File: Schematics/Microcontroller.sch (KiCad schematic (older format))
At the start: 21 parts, among them CON301 USB-MICRO-B, IC301 ATXMEGA256A3BU-A, J301 AVR_JTAG_Header, X301 12MHz, X302 32.768KhZ

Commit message: LEDs are placed!
Worked out how to script KiCAD to do it too. Winner winner, time for a chicken dinner
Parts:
- renumbered BT301 to BT1, C301 to C10, C302 to C11, C303 to C12, C304 to C13, C305 to C14, C306 to C15, C307 to C16, C308 to C17, C309 to C18, C310 to C19, C311 to C20, CON301 to CON1, IC301 to IC1, J301 to J1, R301 to R15, R302 to R16, R303 to R17, R304 to R18, X301 to X1, X302 to X2
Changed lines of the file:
@@
 $EndDescr
 $Comp
-L ATXMEGA256A3BU-A IC301
+L ATXMEGA256A3BU-A IC1
 U 1 1 54B11B55
 P 5850 3550
-F 0 "IC301" H 4900 5350 40  0000 L BNN
+F 0 "IC1" H 4900 5350 40  0000 L BNN
 F 1 "ATXMEGA256A3BU-A" H 6250 1650 40  0000 L BNN
 F 2 "SMD_Packages:TQFP-64" H 5850 3550 35  0000 C CIN
@@
 $EndComp
 $Comp
-L AVR_JTAG_Header J301
+L AVR_JTAG_Header J1
 U 1 1 54B11B88
 P 9350 3150
-F 0 "J301" H 9150 3550 60  0000 C CNN
+F 0 "J1" H 9150 3550 60  0000 C CNN
 F 1 "AVR_JTAG_Header" H 9900 2850 60  0000 C CNN
 F 2 "Socket_Strips:Socket_Strip_Straight_2x05" H 9350 3150 60  0001 C CNN
@@
 $EndComp
 $Comp
-L R R303
+L R R17
 U 1 1 54B11BE7
 P 9050 1550
-F 0 "R303" V 9130 1550 40  0000 C CNN
+F 0 "R17" V 9130 1550 40  0000 C CNN
 F 1 "47k" V 9057 1551 40  0000 C CNN
 F 2 "Resistors_SMD:R_0603" V 8980 1550 30  0001 C CNN
@@
 $EndComp
 $Comp
-L R R304
+L R R18
 U 1 1 54B11C1B
 P 9400 1550
-F 0 "R304" V 9480 1550 40  0000 C CNN
+F 0 "R18" V 9480 1550 40  0000 C CNN
 F 1 "47k" V 9407 1551 40  0000 C CNN
 F 2 "Resistors_SMD:R_0603" V 9330 1550 30  0001 C CNN
@@
 	4250 1950 4750 1950
 $Comp
-L CRYSTAL X302
+L CRYSTAL X2
 U 1 1 54B1373C
 P 3800 2550
-F 0 "X302" H 3800 2700 60  0000 C CNN
+F 0 "X2" H 3800 2700 60  0000 C CNN
 F 1 "32.768KhZ" H 3800 2400 60  0000 C CNN
 F 2 "" H 3800 2550 60  0001 C CNN
@@
 $EndComp
 $Comp
-L C C304
+L C C13
 U 1 1 54B13791
 P 4200 2800
-F 0 "C304" H 4200 2900 40  0000 L CNN
+F 0 "C13" H 4200 2900 40  0000 L CNN
 F 1 "C" H 4206 2715 40  0000 L CNN
 F 2 "Capacitors_SMD:C_0603" H 4238 2650 30  0001 C CNN
@@
 $EndComp
 $Comp
-L C C302
+L C C11
 U 1 1 54B137B6
 P 3400 2800
-F 0 "C302" H 3400 2900 40  0000 L CNN
+F 0 "C11" H 3400 2900 40  0000 L CNN
 F 1 "C" H 3406 2715 40  0000 L CNN
 F 2 "Capacitors_SMD:C_0603" H 3438 2650 30  0001 C CNN
@@
 	3400 3100 3400 3000
 $Comp
-L CRYSTAL X301
+L CRYSTAL X1
 U 1 1 54B13F67
 P 3550 3650
-F 0 "X301" H 3550 3800 60  0000 C CNN
+F 0 "X1" H 3550 3800 60  0000 C CNN
 F 1 "12MHz" H 3550 3500 60  0000 C CNN
 F 2 "" H 3550 3650 60  0001 C CNN
@@
 $EndComp
 $Comp
-L C C303
+L C C12
 U 1 1 54B13F6D
 P 3950 3900
-F 0 "C303" H 3950 4000 40  0000 L CNN
+F 0 "C12" H 3950 4000 40  0000 L CNN
 F 1 "C" H 3956 3815 40  0000 L CNN
 F 2 "Capacitors_SMD:C_0603" H 3988 3750 30  0001 C CNN
@@
 $EndComp
 $Comp
-L C C301
+L C C10
 U 1 1 54B13F73
 P 3150 3900
-F 0 "C301" H 3150 4000 40  0000 L CNN
+F 0 "C10" H 3150 4000 40  0000 L CNN
 F 1 "C" H 3156 3815 40  0000 L CNN
 F 2 "Capacitors_SMD:C_0603" H 3188 3750 30  0001 C CNN
@@
 USB_D-
 $Comp
-L USB-MICRO-B CON301
+L USB-MICRO-B CON1
 U 1 1 54B1509B
 P 9900 5550
-F 0 "CON301" H 9600 5900 50  0000 C CNN
+F 0 "CON1" H 9600 5900 50  0000 C CNN
 F 1 "USB-MICRO-B" H 9750 5200 50  0000 C CNN
 F 2 "Connect:USB_Micro-B" H 9900 5450 50  0001 C CNN
@@
 USB_D-
 $Comp
-L BATTERY BT301
+L BATTERY BT1
 U 1 1 54B172FA
 P 3600 2100
-F 0 "BT301" H 3600 2300 50  0000 C CNN
+F 0 "BT1" H 3600 2300 50  0000 C CNN
 F 1 "3V" H 3600 1910 50  0000 C CNN
 F 2 "" H 3600 2100 60  0001 C CNN
@@
 $EndComp
 $Comp
-L R R301
+L R R15
 U 1 1 54B17628
 P 4350 2250
-F 0 "R301" V 4430 2250 40  0000 C CNN
+F 0 "R15" V 4430 2250 40  0000 C CNN
 F 1 "100R" V 4357 2251 40  0000 C CNN
 F 2 "Resistors_SMD:R_0603" V 4280 2250 30  0001 C CNN
@@
 NoConn ~ 4750 2050
 $Comp
-L R R302
+L R R16
 U 1 1 54B182E1
 P 7200 1000
-F 0 "R302" V 7280 1000 40  0000 C CNN
+F 0 "R16" V 7280 1000 40  0000 C CNN
 F 1 "50R" V 7207 1001 40  0000 C CNN
 F 2 "Resistors_SMD:R_0603" V 7130 1000 30  0001 C CNN
@@
 ~OE[1..12]
 $Comp
-L C C306
+L C C15
 U 1 1 54B28316
 P 4500 1200
-F 0 "C306" H 4500 1300 40  0000 L CNN
+F 0 "C15" H 4500 1300 40  0000 L CNN
 F 1 "100n" H 4506 1115 40  0000 L CNN
 F 2 "Capacitors_SMD:C_0603" H 4538 1050 30  0001 C CNN
@@
 $EndComp
 $Comp
-L C C307
+L C C16
 U 1 1 54B28394
 P 4750 1200
-F 0 "C307" H 4750 1300 40  0000 L CNN
+F 0 "C16" H 4750 1300 40  0000 L CNN
 F 1 "100n" H 4756 1115 40  0000 L CNN
 F 2 "Capacitors_SMD:C_0603" H 4788 1050 30  0001 C CNN
@@
 $EndComp
 $Comp
-L C C308
+L C C17
 U 1 1 54B283DE
 P 5000 1200
-F 0 "C308" H 5000 1300 40  0000 L CNN
+F 0 "C17" H 5000 1300 40  0000 L CNN
 F 1 "100n" H 5006 1115 40  0000 L CNN
 F 2 "Capacitors_SMD:C_0603" H 5038 1050 30  0001 C CNN
@@
 $EndComp
 $Comp
-L C C309
+L C C18
 U 1 1 54B28409
 P 5250 1200
-F 0 "C309" H 5250 1300 40  0000 L CNN
+F 0 "C18" H 5250 1300 40  0000 L CNN
 F 1 "100n" H 5256 1115 40  0000 L CNN
 F 2 "Capacitors_SMD:C_0603" H 5288 1050 30  0001 C CNN
@@
 $EndComp
 $Comp
-L C C310
+L C C19
 U 1 1 54B28435
 P 5500 1200
-F 0 "C310" H 5500 1300 40  0000 L CNN
+F 0 "C19" H 5500 1300 40  0000 L CNN
 F 1 "100n" H 5506 1115 40  0000 L CNN
 F 2 "Capacitors_SMD:C_0603" H 5538 1050 30  0001 C CNN
@@
 $EndComp
 $Comp
-L C C305
+L C C14
 U 1 1 54B28462
 P 4250 1200
-F 0 "C305" H 4250 1300 40  0000 L CNN
+F 0 "C14" H 4250 1300 40  0000 L CNN
 F 1 "1u" H 4256 1115 40  0000 L CNN
 F 2 "Capacitors_SMD:C_0603" H 4288 1050 30  0001 C CNN
@@
 Connection ~ 4250 1500
 $Comp
-L C C311
+L C C20
 U 1 1 54B28ED0
 P 8700 5600
-F 0 "C311" H 8700 5700 40  0000 L CNN
+F 0 "C20" H 8700 5700 40  0000 L CNN
 F 1 "1u" H 8706 5515 40  0000 L CNN
 F 2 "Capacitors_SMD:C_0603" H 8738 5450 30  0001 C CNN

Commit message: Latest schematics and pcb.
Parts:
- removed X1: 12MHz, symbol CRYSTAL
- removed X2: 32.768KhZ, symbol CRYSTAL
- added JP1: JUMPER, symbol JUMPER
- added R100: 100k, Resistors_SMD:R_0603, symbol R
- added X1: 12MHz, symbol CRYSTAL_SMD
- added X2: 32.768KhZ, symbol CRYSTAL_SMD
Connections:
- wire segments 108 -> 115
- no-connect marks 25 -> 23
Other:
- moved on the sheet: R16
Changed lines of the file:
@@
 	4250 1950 4750 1950
-$Comp
-L CRYSTAL X2
-U 1 1 54B1373C
-P 3800 2550
-F 0 "X2" H 3800 2700 60  0000 C CNN
-F 1 "32.768KhZ" H 3800 2400 60  0000 C CNN
-F 2 "" H 3800 2550 60  0001 C CNN
-F 3 "" H 3800 2550 60  0000 C CNN
-	1    3800 2550
-	1    0    0    -1
-$EndComp
 $Comp
 L C C13
@@
 $EndComp
 Wire Wire Line
-	4100 2550 4750 2550
+	4000 2550 4750 2550
 Connection ~ 4200 2550
 Wire Wire Line
@@
 	3400 2600 3400 2550
 Wire Wire Line
-	3250 2550 3500 2550
+	3250 2550 3600 2550
 Connection ~ 3400 2550
 Text Label 4500 2750 0    60   ~ 0
@@
 	3400 3100 3400 3000
 $Comp
-L CRYSTAL X1
-U 1 1 54B13F67
-P 3550 3650
-F 0 "X1" H 3550 3800 60  0000 C CNN
-F 1 "12MHz" H 3550 3500 60  0000 C CNN
-F 2 "" H 3550 3650 60  0001 C CNN
-F 3 "" H 3550 3650 60  0000 C CNN
-	1    3550 3650
-	1    0    0    -1
-$EndComp
-$Comp
 L C C12
 U 1 1 54B13F6D
@@
 	3150 3700 3150 3650
 Wire Wire Line
-	3000 3650 3250 3650
+	3000 3650 3350 3650
 Connection ~ 3150 3650
 $Comp
@@
 	3150 4200 3150 4100
 Wire Wire Line
-	3850 3650 4450 3650
+	3750 3650 4450 3650
 Wire Wire Line
 	4450 3650 4450 3400
@@
 L R R16
 U 1 1 54B182E1
-P 7200 1000
-F 0 "R16" V 7280 1000 40  0000 C CNN
-F 1 "50R" V 7207 1001 40  0000 C CNN
-F 2 "Resistors_SMD:R_0603" V 7130 1000 30  0001 C CNN
-F 3 "" H 7200 1000 30  0000 C CNN
-	1    7200 1000
-	1    0    0    -1
-$EndComp
-Text HLabel 7500 700  2    60   Input ~ 0
+P 7850 1000
+F 0 "R16" V 7930 1000 40  0000 C CNN
+F 1 "50R" V 7857 1001 40  0000 C CNN
+F 2 "Resistors_SMD:R_0603" V 7780 1000 30  0001 C CNN
+F 3 "" H 7850 1000 30  0000 C CNN
+	1    7850 1000
+	1    0    0    -1
+$EndComp
+Text HLabel 8150 700  2    60   Input ~ 0
 RF_In
 $Comp
 L GND #PWR030
 U 1 1 54B18749
-P 7200 1300
-F 0 "#PWR030" H 7200 1050 60  0001 C CNN
-F 1 "GND" H 7200 1150 60  0000 C CNN
-F 2 "" H 7200 1300 60  0000 C CNN
-F 3 "" H 7200 1300 60  0000 C CNN
-	1    7200 1300
-	1    0    0    -1
-$EndComp
-Wire Wire Line
-	6950 1950 7450 1950
-Wire Wire Line
-	7050 700  7500 700
-Wire Wire Line
-	7200 750  7200 700
-Connection ~ 7200 700
-Text Label 7050 700  2    60   ~ 0
+P 7850 1300
+F 0 "#PWR030" H 7850 1050 60  0001 C CNN
+F 1 "GND" H 7850 1150 60  0000 C CNN
+F 2 "" H 7850 1300 60  0000 C CNN
+F 3 "" H 7850 1300 60  0000 C CNN
+	1    7850 1300
+	1    0    0    -1
+$EndComp
+Wire Wire Line
+	7700 700  8150 700
+Wire Wire Line
+	7850 750  7850 700
+Connection ~ 7850 700
+Text Label 7700 700  2    60   ~ 0
 RF_In
-Text Label 7450 1950 2    60   ~ 0
+Text Label 7400 2650 2    60   ~ 0
 RF_In
 Wire Wire Line
-	7200 1300 7200 1250
+	7850 1300 7850 1250
 NoConn ~ 6950 2050
 NoConn ~ 6950 2150
-NoConn ~ 6950 2250
 NoConn ~ 6950 2350
 NoConn ~ 6950 2450
 NoConn ~ 6950 2550
-NoConn ~ 6950 2650
 NoConn ~ 6950 2800
 NoConn ~ 6950 2900
@@
 NoConn ~ 4750 4800
 NoConn ~ 4750 4900
-NoConn ~ 4750 5000
 Text Label 8050 5100 2    60   ~ 0
 ~OE[1..12]
@@
 	8700 5800 9250 5800
 Connection ~ 9250 5800
+$Comp
+L CRYSTAL_SMD X2
+U 1 1 54B2624B
+P 3800 2550
+F 0 "X2" H 3800 2640 30  0000 C CNN
+F 1 "32.768KhZ" H 3830 2440 30  0000 L CNN
+F 2 "" H 3800 2550 60  0000 C CNN
+F 3 "" H 3800 2550 60  0000 C CNN
+	1    3800 2550
+	1    0    0    -1
+$EndComp
+$Comp
+L GND #PWR033
+U 1 1 54B26812
+P 3800 2700
+F 0 "#PWR033" H 3800 2450 60  0001 C CNN
+F 1 "GND" H 3800 2550 60  0000 C CNN
+F 2 "" H 3800 2700 60  0000 C CNN
+F 3 "" H 3800 2700 60  0000 C CNN
+	1    3800 2700
+	1    0    0    -1
+$EndComp
+Wire Wire Line
+	3800 2700 3800 2650
+$Comp
+L CRYSTAL_SMD X1
+U 1 1 54B26940
+P 3550 3650
+F 0 "X1" H 3550 3740 30  0000 C CNN
+F 1 "12MHz" H 3580 3540 30  0000 L CNN
+F 2 "" H 3550 3650 60  0000 C CNN
+F 3 "" H 3550 3650 60  0000 C CNN
+	1    3550 3650
+	1    0    0    -1
+$EndComp
+$Comp
+L GND #PWR034
+U 1 1 54B26B40
+P 3550 3850
+F 0 "#PWR034" H 3550 3600 60  0001 C CNN
+F 1 "GND" H 3550 3700 60  0000 C CNN
+F 2 "" H 3550 3850 60  0000 C CNN
+F 3 "" H 3550 3850 60  0000 C CNN
+	1    3550 3850
+	1    0    0    -1
+$EndComp
+Wire Wire Line
+	3550 3850 3550 3750
+Wire Wire Line
+	6950 2650 7400 2650
+$Comp
+L JUMPER JP1
+U 1 1 54B2854F
+P 7450 2250
+F 0 "JP1" H 7450 2400 60  0000 C CNN
+F 1 "JUMPER" H 7450 2170 40  0000 C CNN
+F 2 "" H 7450 2250 60  0000 C CNN
+F 3 "" H 7450 2250 60  0000 C CNN
+	1    7450 2250
+	1    0    0    -1
+$EndComp
+NoConn ~ 6950 1950
+$Comp
+L GND #PWR035
+U 1 1 54B2A340
+P 7800 2350
+F 0 "#PWR035" H 7800 2100 60  0001 C CNN
+F 1 "GND" H 7800 2200 60  0000 C CNN
+F 2 "" H 7800 2350 60  0000 C CNN
+F 3 "" H 7800 2350 60  0000 C CNN
+	1    7800 2350
+	1    0    0    -1
+$EndComp
+$Comp
+L R R100
+U 1 1 54B2AC08
+P 7100 1950
+F 0 "R100" V 7180 1950 40  0000 C CNN
+F 1 "100k" V 7107 1951 40  0000 C CNN
+F 2 "Resistors_SMD:R_0603" V 7030 1950 30  0001 C CNN
+F 3 "" H 7100 1950 30  0000 C CNN
+	1    7100 1950
+	1    0    0    -1
+$EndComp
+$Comp
+L VPP #PWR036
+U 1 1 54B2B24F
+P 7100 1650
+F 0 "#PWR036" H 7100 1500 60  0001 C CNN
+F 1 "VPP" H 7100 1800 60  0000 C CNN
+F 2 "" H 7100 1650 60  0000 C CNN
+F 3 "" H 7100 1650 60  0000 C CNN
+	1    7100 1650
+	1    0    0    -1
+$EndComp
+Wire Wire Line
+	7100 1700 7100 1650
+Wire Wire Line
+	6950 2250 7150 2250
+Wire Wire Line
+	7100 2200 7100 2250
+Connection ~ 7100 2250
+Wire Wire Line
+	7800 2350 7800 2250
+Wire Wire Line
+	7800 2250 7750 2250
 $EndSCHEMATC

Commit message: Updated schematics
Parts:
- removed R16: 50R, Resistors_SMD:R_0603, symbol R
- added P?: CONN_02X08, symbol CONN_02X08
- BT1: footprint (none) -> rgb:BU2032SM-HD-GTR-ND
- CON1: footprint Connect:USB_Micro-B -> usb:USB_Micro-B
- IC1: footprint SMD_Packages:TQFP-64 -> Housings_QFP:TQFP-64_14x14mm_Pitch0.8mm
- J1: footprint Socket_Strips:Socket_Strip_Straight_2x05 -> rgb:FTSH-105-01-L-DV-K-A-P
- JP1: footprint (none) -> SMD_Packages:SMD-0201_r
- X1, X2: footprint (none) -> Crystals_Oscillators_SMD:crystal_FA238-TSX3225
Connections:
- net labels added: MISO, MOSI, RX, SCK, TX, Vusb, ~CS
- net labels removed: RF_In
- wire segments 115 -> 126
- no-connect marks 23 -> 20
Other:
- moved on the sheet: C10, C12, JP1, R100, X1

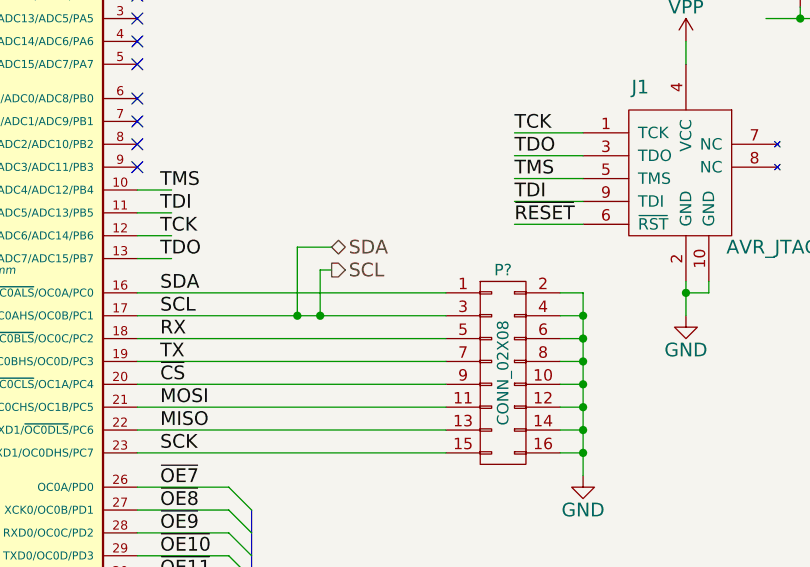
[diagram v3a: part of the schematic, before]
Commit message: Removed RF. Placed all LED drivers and passives and begun routing
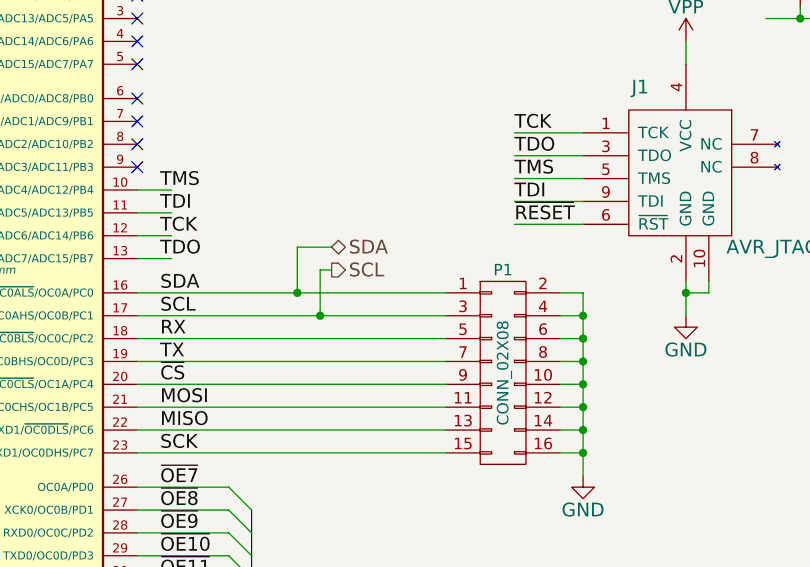
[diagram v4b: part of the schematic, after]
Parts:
- gave numbers to parts that had none: 1
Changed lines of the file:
@@
 SCL
 $Comp
-L VPP #PWR019
+L VPP #PWR02
 U 1 1 54B121F9
 P 9250 1200
-F 0 "#PWR019" H 9250 1050 60  0001 C CNN
+F 0 "#PWR02" H 9250 1050 60  0001 C CNN
 F 1 "VPP" H 9250 1350 60  0000 C CNN
 F 2 "" H 9250 1200 60  0000 C CNN
@@
 $EndComp
 $Comp
-L VPP #PWR020
+L VPP #PWR03
 U 1 1 54B1220F
 P 5800 1450
-F 0 "#PWR020" H 5800 1300 60  0001 C CNN
+F 0 "#PWR03" H 5800 1300 60  0001 C CNN
 F 1 "VPP" H 5800 1600 60  0000 C CNN
 F 2 "" H 5800 1450 60  0000 C CNN
@@
 $EndComp
 $Comp
-L GND #PWR021
+L GND #PWR04
 U 1 1 54B12386
 P 5850 5600
-F 0 "#PWR021" H 5850 5350 60  0001 C CNN
+F 0 "#PWR04" H 5850 5350 60  0001 C CNN
 F 1 "GND" H 5850 5450 60  0000 C CNN
 F 2 "" H 5850 5600 60  0000 C CNN
@@
 TMS
 $Comp
-L VPP #PWR022
+L VPP #PWR05
 U 1 1 54B12F47
 P 9350 2550
-F 0 "#PWR022" H 9350 2400 60  0001 C CNN
+F 0 "#PWR05" H 9350 2400 60  0001 C CNN
 F 1 "VPP" H 9350 2700 60  0000 C CNN
 F 2 "" H 9350 2550 60  0000 C CNN
@@
 $EndComp
 $Comp
-L GND #PWR023
+L GND #PWR06
 U 1 1 54B12FD2
 P 9350 3750
-F 0 "#PWR023" H 9350 3500 60  0001 C CNN
+F 0 "#PWR06" H 9350 3500 60  0001 C CNN
 F 1 "GND" H 9350 3600 60  0000 C CNN
 F 2 "" H 9350 3750 60  0000 C CNN
@@
 TOSC1
 $Comp
-L GND #PWR024
+L GND #PWR07
 U 1 1 54B13B7D
 P 3400 3100
-F 0 "#PWR024" H 3400 2850 60  0001 C CNN
+F 0 "#PWR07" H 3400 2850 60  0001 C CNN
 F 1 "GND" H 3400 2950 60  0000 C CNN
 F 2 "" H 3400 3100 60  0000 C CNN
@@
 $EndComp
 $Comp
-L GND #PWR025
+L GND #PWR08
 U 1 1 54B13BA4
 P 4200 3100
-F 0 "#PWR025" H 4200 2850 60  0001 C CNN
+F 0 "#PWR08" H 4200 2850 60  0001 C CNN
 F 1 "GND" H 4200 2950 60  0000 C CNN
 F 2 "" H 4200 3100 60  0000 C CNN
@@
 $EndComp
 $Comp
-L GND #PWR026
+L GND #PWR09
 U 1 1 54B13F80
 P 3150 3900
-F 0 "#PWR026" H 3150 3650 60  0001 C CNN
+F 0 "#PWR09" H 3150 3650 60  0001 C CNN
 F 1 "GND" H 3150 3750 60  0000 C CNN
 F 2 "" H 3150 3900 60  0000 C CNN
@@
 $EndComp
 $Comp
-L GND #PWR027
+L GND #PWR010
 U 1 1 54B13F86
 P 3950 3900
-F 0 "#PWR027" H 3950 3650 60  0001 C CNN
+F 0 "#PWR010" H 3950 3650 60  0001 C CNN
 F 1 "GND" H 3950 3750 60  0000 C CNN
 F 2 "" H 3950 3900 60  0000 C CNN
@@
 $EndComp
 $Comp
-L GND #PWR028
+L GND #PWR011
 U 1 1 54B15BE6
 P 9250 5850
-F 0 "#PWR028" H 9250 5600 60  0001 C CNN
+F 0 "#PWR011" H 9250 5600 60  0001 C CNN
 F 1 "GND" H 9250 5700 60  0000 C CNN
 F 2 "" H 9250 5850 60  0000 C CNN
@@
 $EndComp
 $Comp
-L GND #PWR029
+L GND #PWR012
 U 1 1 54B15BFC
 P 10450 5850
-F 0 "#PWR029" H 10450 5600 60  0001 C CNN
+F 0 "#PWR012" H 10450 5600 60  0001 C CNN
 F 1 "GND" H 10450 5700 60  0000 C CNN
 F 2 "" H 10450 5850 60  0000 C CNN
@@
 $EndComp
 $Comp
-L GND #PWR030
+L GND #PWR013
 U 1 1 54B17721
 P 3200 2200
-F 0 "#PWR030" H 3200 1950 60  0001 C CNN
+F 0 "#PWR013" H 3200 1950 60  0001 C CNN
 F 1 "GND" H 3200 2050 60  0000 C CNN
 F 2 "" H 3200 2200 60  0000 C CNN
@@
 $EndComp
 $Comp
-L VPP #PWR032
+L VPP #PWR014
 U 1 1 54B284BD
 P 4900 900
-F 0 "#PWR032" H 4900 750 60  0001 C CNN
+F 0 "#PWR014" H 4900 750 60  0001 C CNN
 F 1 "VPP" H 4900 1050 60  0000 C CNN
 F 2 "" H 4900 900 60  0000 C CNN
@@
 $EndComp
 $Comp
-L GND #PWR033
+L GND #PWR015
 U 1 1 54B28C09
 P 4250 1600
-F 0 "#PWR033" H 4250 1350 60  0001 C CNN
+F 0 "#PWR015" H 4250 1350 60  0001 C CNN
 F 1 "GND" H 4250 1450 60  0000 C CNN
 F 2 "" H 4250 1600 60  0000 C CNN
@@
 $EndComp
 $Comp
-L GND #PWR034
+L GND #PWR016
 U 1 1 54B26812
 P 3800 2700
-F 0 "#PWR034" H 3800 2450 60  0001 C CNN
+F 0 "#PWR016" H 3800 2450 60  0001 C CNN
 F 1 "GND" H 3800 2550 60  0000 C CNN
 F 2 "" H 3800 2700 60  0000 C CNN
@@
 $EndComp
 $Comp
-L GND #PWR035
+L GND #PWR017
 U 1 1 54B26B40
 P 3550 3600
-F 0 "#PWR035" H 3550 3350 60  0001 C CNN
+F 0 "#PWR017" H 3550 3350 60  0001 C CNN
 F 1 "GND" H 3550 3450 60  0000 C CNN
 F 2 "" H 3550 3600 60  0000 C CNN
@@
 $EndComp
 $Comp
-L GND #PWR036
+L GND #PWR018
 U 1 1 54B2A340
 P 10550 2550
-F 0 "#PWR036" H 10550 2300 60  0001 C CNN
+F 0 "#PWR018" H 10550 2300 60  0001 C CNN
 F 1 "GND" H 10550 2400 60  0000 C CNN
 F 2 "" H 10550 2550 60  0000 C CNN
@@
 $EndComp
 $Comp
-L VPP #PWR037
+L VPP #PWR019
 U 1 1 54B2B24F
 P 9850 1850
-F 0 "#PWR037" H 9850 1700 60  0001 C CNN
+F 0 "#PWR019" H 9850 1700 60  0001 C CNN
 F 1 "VPP" H 9850 2000 60  0000 C CNN
 F 2 "" H 9850 1850 60  0000 C CNN
@@
 NoConn ~ 6950 1950
 $Comp
-L CONN_02X08 P?
+L CONN_02X08 P1
 U 1 1 54C8095F
 P 8550 4000
-F 0 "P?" H 8550 4450 50  0000 C CNN
+F 0 "P1" H 8550 4450 50  0000 C CNN
 F 1 "CONN_02X08" V 8550 4000 50  0000 C CNN
 F 2 "" H 8550 2800 60  0000 C CNN
@@
 $EndComp
 $Comp
-L GND #PWR?
+L GND #PWR020
 U 1 1 54C80C62
 P 8900 4450
-F 0 "#PWR?" H 8900 4200 60  0001 C CNN
+F 0 "#PWR020" H 8900 4200 60  0001 C CNN
 F 1 "GND" H 8900 4300 60  0000 C CNN
 F 2 "" H 8900 4450 60  0000 C CNN
@@
 Connection ~ 7750 3750
 Wire Wire Line
-	7650 3750 7650 3450
-Wire Wire Line
 	7650 3450 7800 3450
-Connection ~ 7650 3750
+Wire Wire Line
+	7650 3450 7650 3650
+Connection ~ 7650 3650
 $EndSCHEMATC
